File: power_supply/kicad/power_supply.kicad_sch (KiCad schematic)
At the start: 19 parts, among them J1 pcie_98, J2 Conn_01x05_Socket, U1 URB2405YMD-10WR3, U2 ESD5344D

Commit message: Fixed part number of 1.25A fuse.
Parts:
- F1, F2: LCSC C21190 -> C163130
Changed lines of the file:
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@@
       (effects (font (size 1.27 1.27)) hide)
     )
-    (property "LCSC" "C21190" (at 107.95 82.55 0)
+    (property "LCSC" "C163130" (at 107.95 82.55 0)
       (effects (font (size 1.27 1.27)))
     )
@@
       (effects (font (size 1.27 1.27)) hide)
     )
-    (property "LCSC" "C21190" (at 107.95 60.96 0)
+    (property "LCSC" "C163130" (at 107.95 60.96 0)
       (effects (font (size 1.27 1.27)))
     )

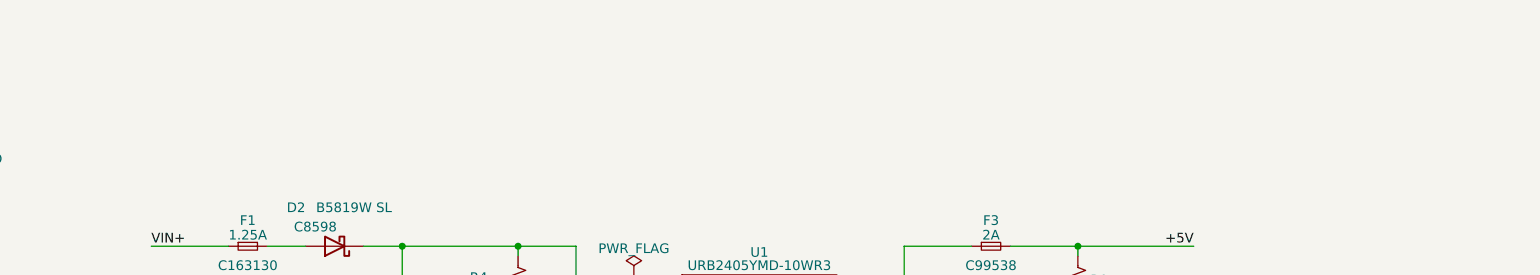
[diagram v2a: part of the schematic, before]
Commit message: Added a TODO to the power supply card's schematic.
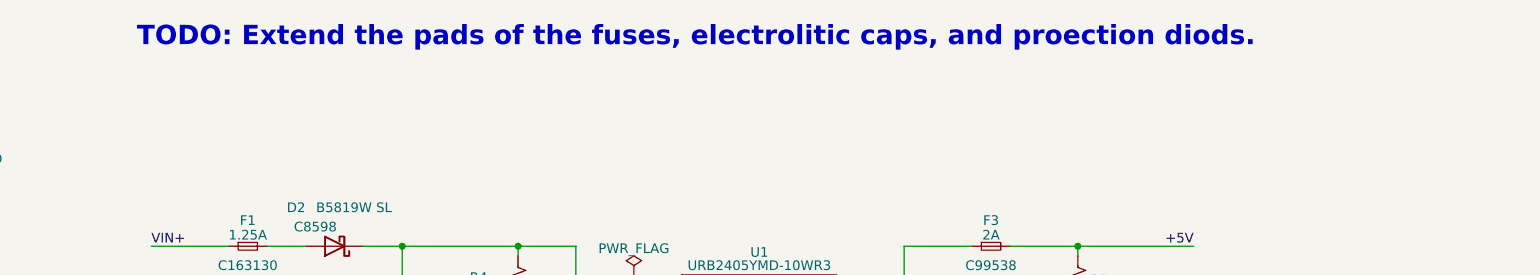
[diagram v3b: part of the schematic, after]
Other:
- note added: "TODO: Extend the pads of the fuses, electrolitic caps, and proection diods."
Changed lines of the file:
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@@
     (effects (font (size 3 3) (thickness 0.6) bold) (justify left bottom))
+  )
+  (text "TODO: Extend the pads of the fuses, electrolitic caps, and proection diods."
+    (at 93.345 32.385 0)
+    (effects (font (size 2.54 2.54) (thickness 0.508) bold (color 255 0 0 1)) (justify left bottom))
   )
   (text "Test Points" (at 201.93 153.67 0)

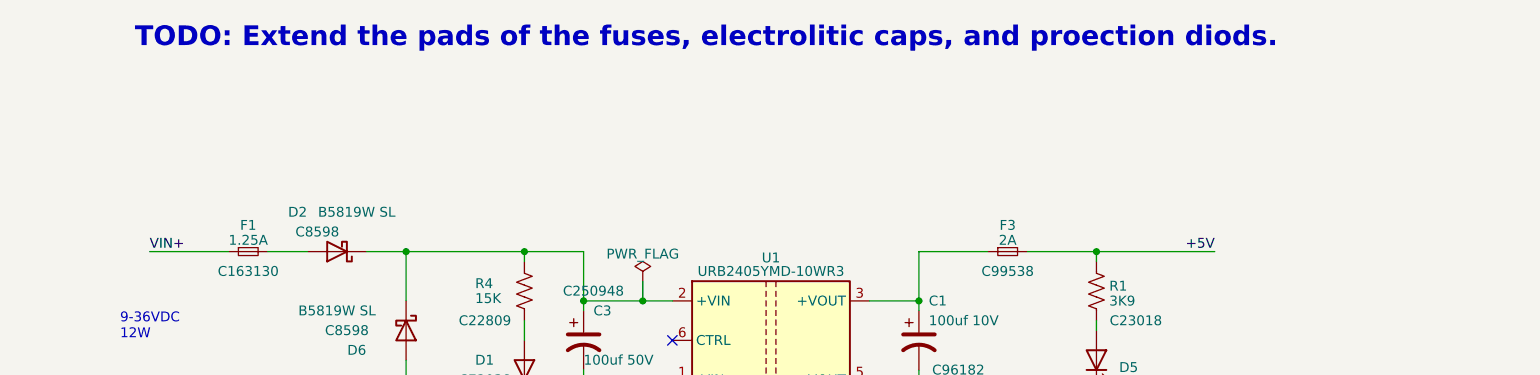
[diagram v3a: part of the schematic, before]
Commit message: Added to the schematic of the power supply a TODO to increase the resistor of the +5V LED.
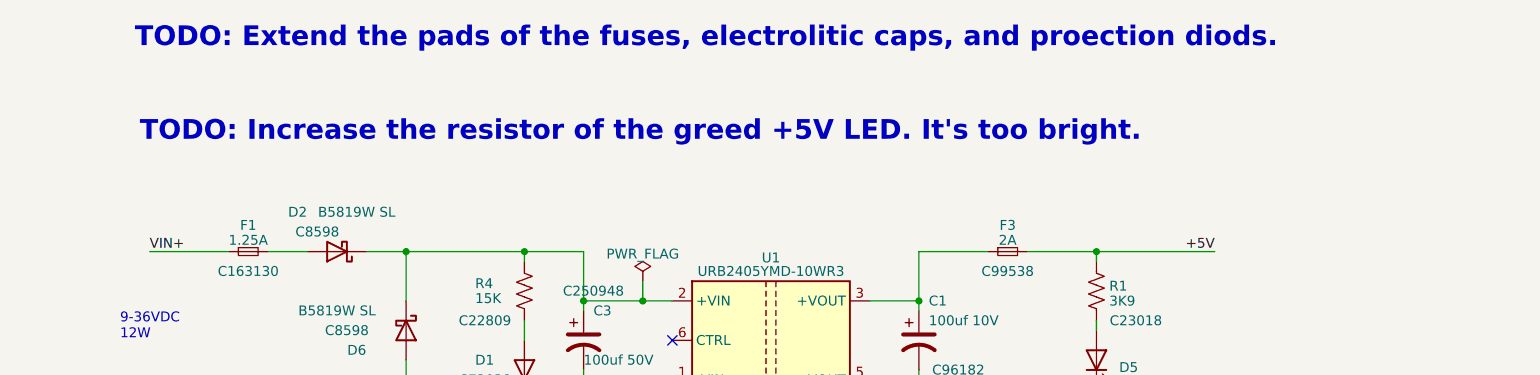
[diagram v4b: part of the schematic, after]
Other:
- note added: "TODO: Increase the resistor of the greed +5V LED. It's too bright."
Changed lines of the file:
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@@
     (effects (font (size 3 3) (thickness 0.6) bold) (justify left bottom))
+  )
+  (text "TODO: Increase the resistor of the greed +5V LED. It's too bright."
+    (at 93.98 44.45 0)
+    (effects (font (size 2.54 2.54) (thickness 0.508) bold (color 255 0 0 1)) (justify left bottom))
   )
   (text "9-36VDC\n12W" (at 91.44 69.85 0)

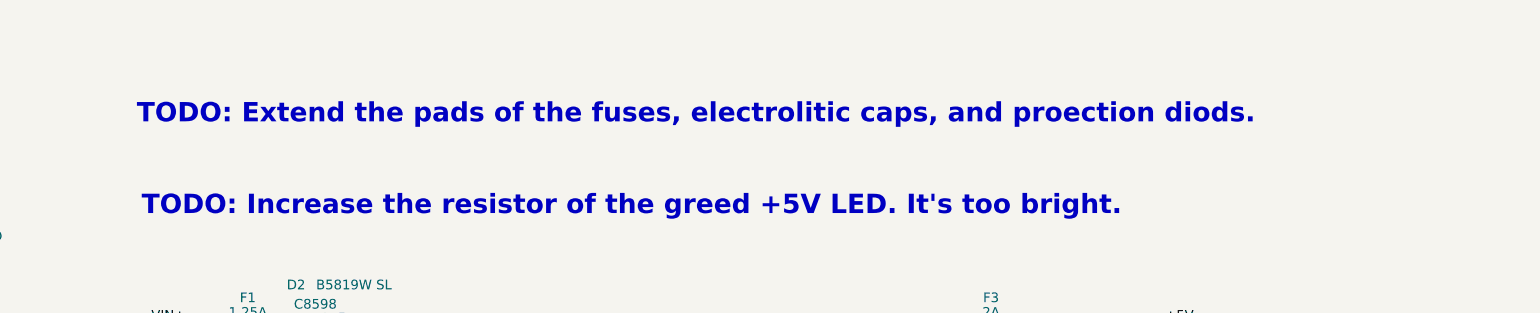
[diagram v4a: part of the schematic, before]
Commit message: Updated controller and power supply schematics.
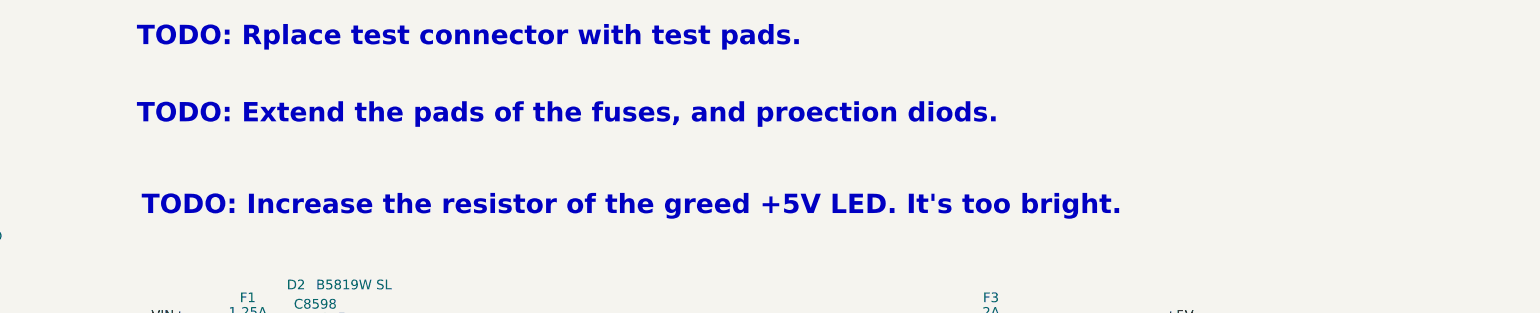
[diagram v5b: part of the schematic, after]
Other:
- note added: "TODO: Extend the pads of the fuses, and proection diods."
- note added: "TODO: Rplace test connector with test pads."
- note removed: "TODO: Extend the pads of the fuses, electrolitic caps, and proection diods."
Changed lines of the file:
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@@
     (effects (font (size 3 3) (thickness 0.6) bold) (justify left bottom))
+  )
+  (text "TODO: Rplace test connector with test pads." (at 93.345 22.225 0)
+    (effects (font (size 2.54 2.54) (thickness 0.508) bold (color 255 0 0 1)) (justify left bottom))
   )
   (text "TODO: Increase the resistor of the greed +5V LED. It's too bright."
@@
     (effects (font (size 3 3) (thickness 0.6) bold) (justify left bottom))
   )
-  (text "TODO: Extend the pads of the fuses, electrolitic caps, and proection diods."
+  (text "TODO: Extend the pads of the fuses, and proection diods."
     (at 93.345 32.385 0)
     (effects (font (size 2.54 2.54) (thickness 0.508) bold (color 255 0 0 1)) (justify left bottom))

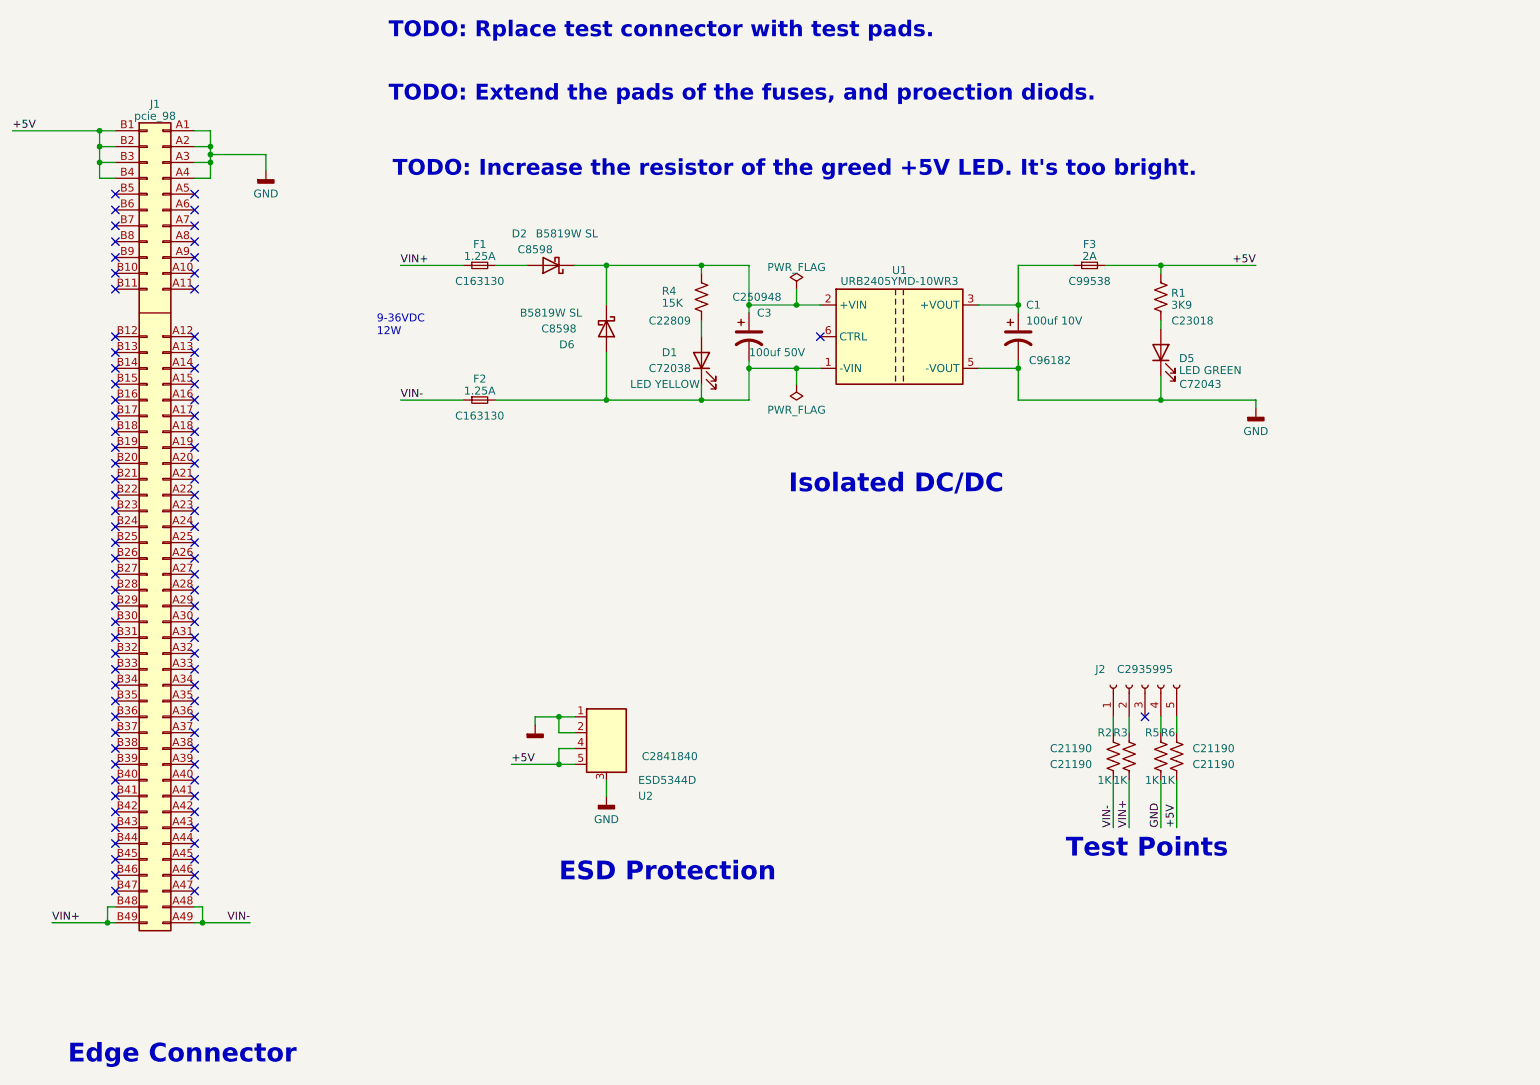
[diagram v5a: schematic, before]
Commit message: Cleaned up TODOs of the power supply board.
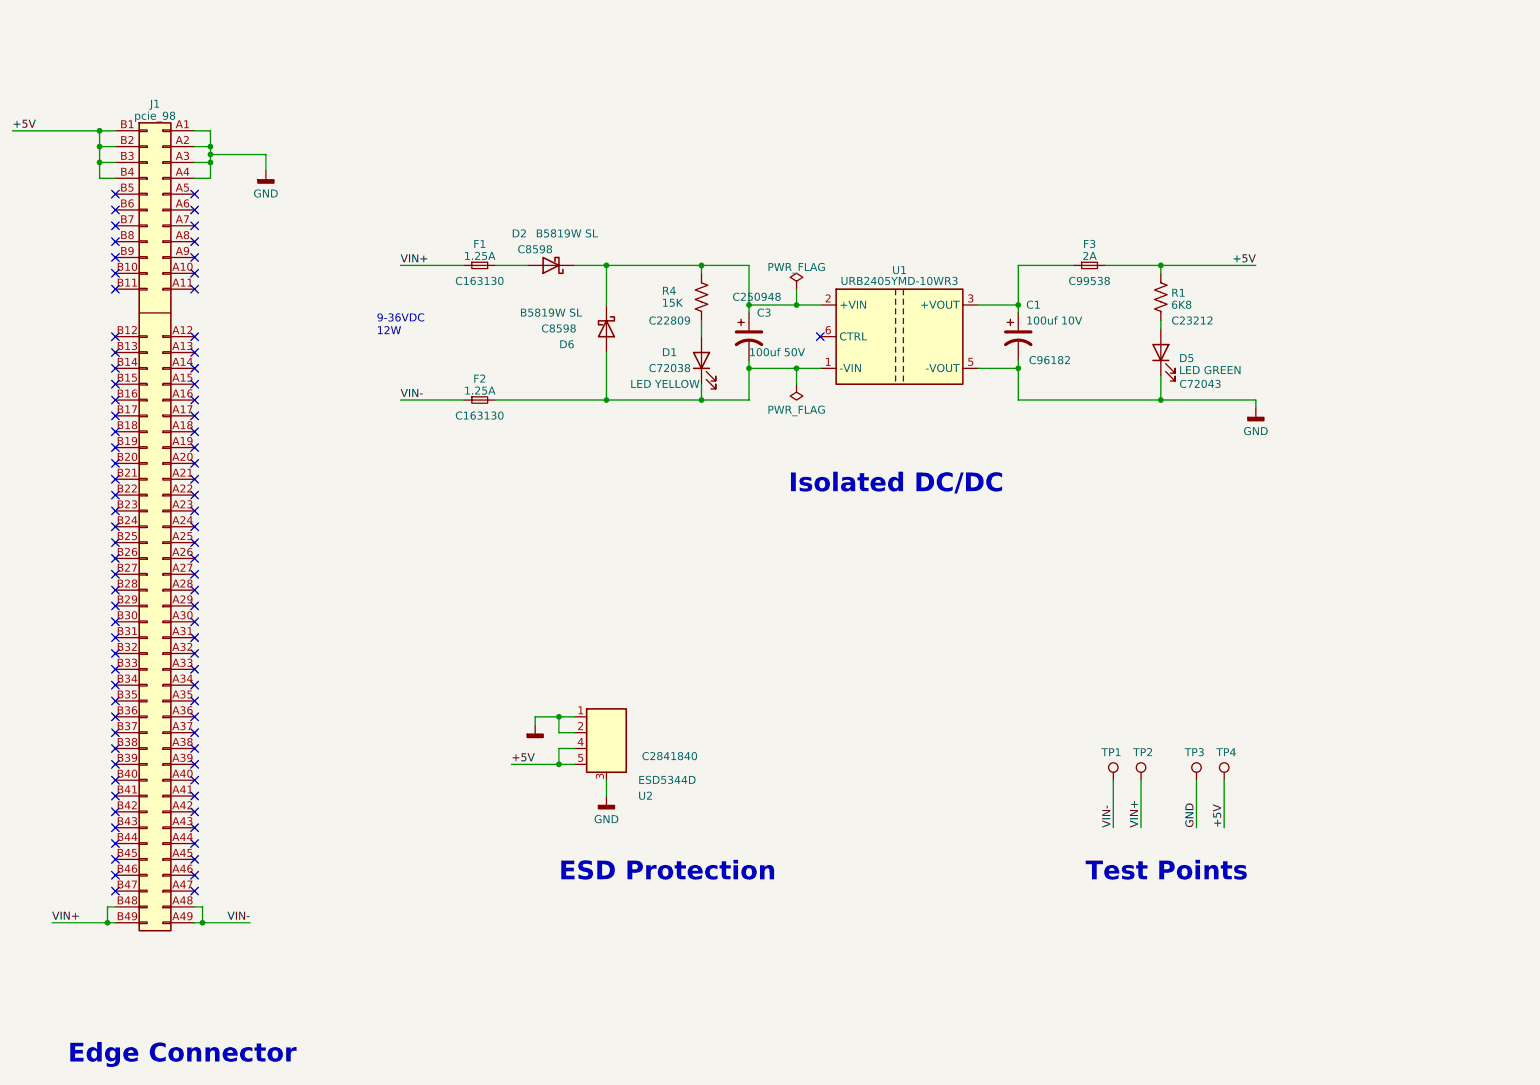
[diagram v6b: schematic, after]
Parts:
- removed J2: Conn_01x05_Socket, common:PinSocket_1x05_P2.54mm_Horizontal_JLCPCB, symbol Connector:Conn_01x05_Socket
- removed R2, R3, R5, R6: 1K, Resistor_SMD:R_0603_1608Metric, symbol Device:R_US
- added TP1, TP2, TP3, TP4: TestPoint, common:Test_Pad, symbol common:TestPoint
- F1, F2, F3: footprint Fuse:Fuse_1206_3216Metric -> Fuse:Fuse_1206_3216Metric_Pad1.42x1.75mm_HandSolder
- R1: value 3K9 -> 6K8; LCSC C23018 -> C23212
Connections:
- net +5V: now also TP4.1
- net GND: now also TP3.1
- net VIN+: now also TP2.1
- net VIN-: now also TP1.1
- no-connect marks 88 -> 87
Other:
- note removed: "TODO: Extend the pads of the fuses, and proection diods."
- note removed: "TODO: Increase the resistor of the greed +5V LED. It's too bright."
- note removed: "TODO: Rplace test connector with test pads."

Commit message: Minor tweak of the schematics.
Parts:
- F1, F2, F3: footprint Fuse:Fuse_1206_3216Metric_Pad1.42x1.75mm_HandSolder -> common:Fuse_1206_3216Metric_Pad1.42x1.75mm_HandSolder
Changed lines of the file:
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@@
 (kicad_sch (version 20230121) (generator eeschema)
   (paper "USLetter")
+  (title_block
+    (rev "0.2")
+  )
   (junction (at 194.31 74.93) (diameter 0) (color 0 0 0 0)
   )
@@
   (junction (at 128.27 80.01) (diameter 0) (color 0 0 0 0)
   )
+  (junction (at 64.77 36.83) (diameter 0) (color 0 0 0 0)
+  )
   (junction (at 158.75 74.93) (diameter 0) (color 0 0 0 0)
   )
@@
   )
   (junction (at 143.51 80.01) (diameter 0) (color 0 0 0 0)
-  )
-  (junction (at 64.77 40.64) (diameter 0) (color 0 0 0 0)
   )
   (junction (at 217.17 58.42) (diameter 0) (color 0 0 0 0)
@@
     (stroke (width 0) (type default))
   )
-  (wire (pts (xy 64.77 40.64) (xy 73.66 40.64))
+  (wire (pts (xy 64.77 36.83) (xy 73.66 36.83))
     (stroke (width 0) (type default))
   )
@@
     (stroke (width 0) (type default))
   )
-  (wire (pts (xy 64.77 39.37) (xy 64.77 40.64))
+  (wire (pts (xy 64.77 39.37) (xy 64.77 41.91))
     (stroke (width 0) (type default))
   )
@@
     (stroke (width 0) (type default))
   )
-  (wire (pts (xy 64.77 40.64) (xy 64.77 41.91))
-    (stroke (width 0) (type default))
-  )
   (wire (pts (xy 46.99 36.83) (xy 49.53 36.83))
     (stroke (width 0) (type default))
@@
     (stroke (width 0) (type default))
   )
-  (wire (pts (xy 73.66 40.64) (xy 73.66 43.18))
+  (wire (pts (xy 73.66 36.83) (xy 73.66 39.37))
     (stroke (width 0) (type default))
   )
@@
       (effects (font (size 1.27 1.27)))
     )
-    (property "Footprint" "Fuse:Fuse_1206_3216Metric_Pad1.42x1.75mm_HandSolder" (at 107.95 80.01 0)
+    (property "Footprint" "common:Fuse_1206_3216Metric_Pad1.42x1.75mm_HandSolder" (at 107.95 80.01 0)
       (effects (font (size 1.27 1.27)) hide)
     )
@@
       (effects (font (size 1.27 1.27)))
     )
-    (property "Footprint" "Fuse:Fuse_1206_3216Metric_Pad1.42x1.75mm_HandSolder" (at 205.74 58.42 0)
+    (property "Footprint" "common:Fuse_1206_3216Metric_Pad1.42x1.75mm_HandSolder" (at 205.74 58.42 0)
       (effects (font (size 1.27 1.27)) hide)
     )
@@
       (effects (font (size 1.27 1.27)))
     )
-    (property "Footprint" "Fuse:Fuse_1206_3216Metric_Pad1.42x1.75mm_HandSolder" (at 107.95 58.42 0)
+    (property "Footprint" "common:Fuse_1206_3216Metric_Pad1.42x1.75mm_HandSolder" (at 107.95 58.42 0)
       (effects (font (size 1.27 1.27)) hide)
     )
@@
     )
   )
-  (symbol (lib_id "common:GND") (at 73.66 43.18 0) (unit 1)
+  (symbol (lib_id "common:GND") (at 73.66 39.37 0) (unit 1)
     (in_bom yes) (on_board yes) (dnp no) (fields_autoplaced)
-    (property "Reference" "#PWR04" (at 73.66 49.53 0)
-      (effects (font (size 1.27 1.27)) hide)
-    )
-    (property "Value" "GND" (at 73.66 46.9345 0)
-      (effects (font (size 1.27 1.27)))
-    )
-    (property "Footprint" "" (at 73.66 43.18 0)
-      (effects (font (size 1.27 1.27)) hide)
-    )
-    (property "Datasheet" "" (at 73.66 43.18 0)
-      (effects (font (size 1.27 1.27)) hide)
-    )
+    (property "Reference" "#PWR04" (at 73.66 45.72 0)
+      (effects (font (size 1.27 1.27)) hide)
+    )
+    (property "Value" "GND" (at 73.66 43.1245 0)
+      (effects (font (size 1.27 1.27)))
+    )
+    (property "Footprint" "" (at 73.66 39.37 0)
+      (effects (font (size 1.27 1.27)) hide)
+    )
+    (property "Datasheet" "" (at 73.66 39.37 0)
+      (effects (font (size 1.27 1.27)) hide)
+    )

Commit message: Added TODOs to Kicad schematics.
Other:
- note added: "TODO: Make the VIN led also red."
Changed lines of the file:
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@@
     (effects (font (size 3 3) (thickness 0.6) bold) (justify left bottom))
+  )
+  (text "TODO: Make the VIN led also red." (at 136.525 34.925 0)
+    (effects (font (size 2.54 2.54) (color 255 0 0 1)) (justify left bottom))
   )
   (text "Test Points" (at 205.105 157.48 0)
